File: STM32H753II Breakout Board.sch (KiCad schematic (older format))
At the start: 23 parts

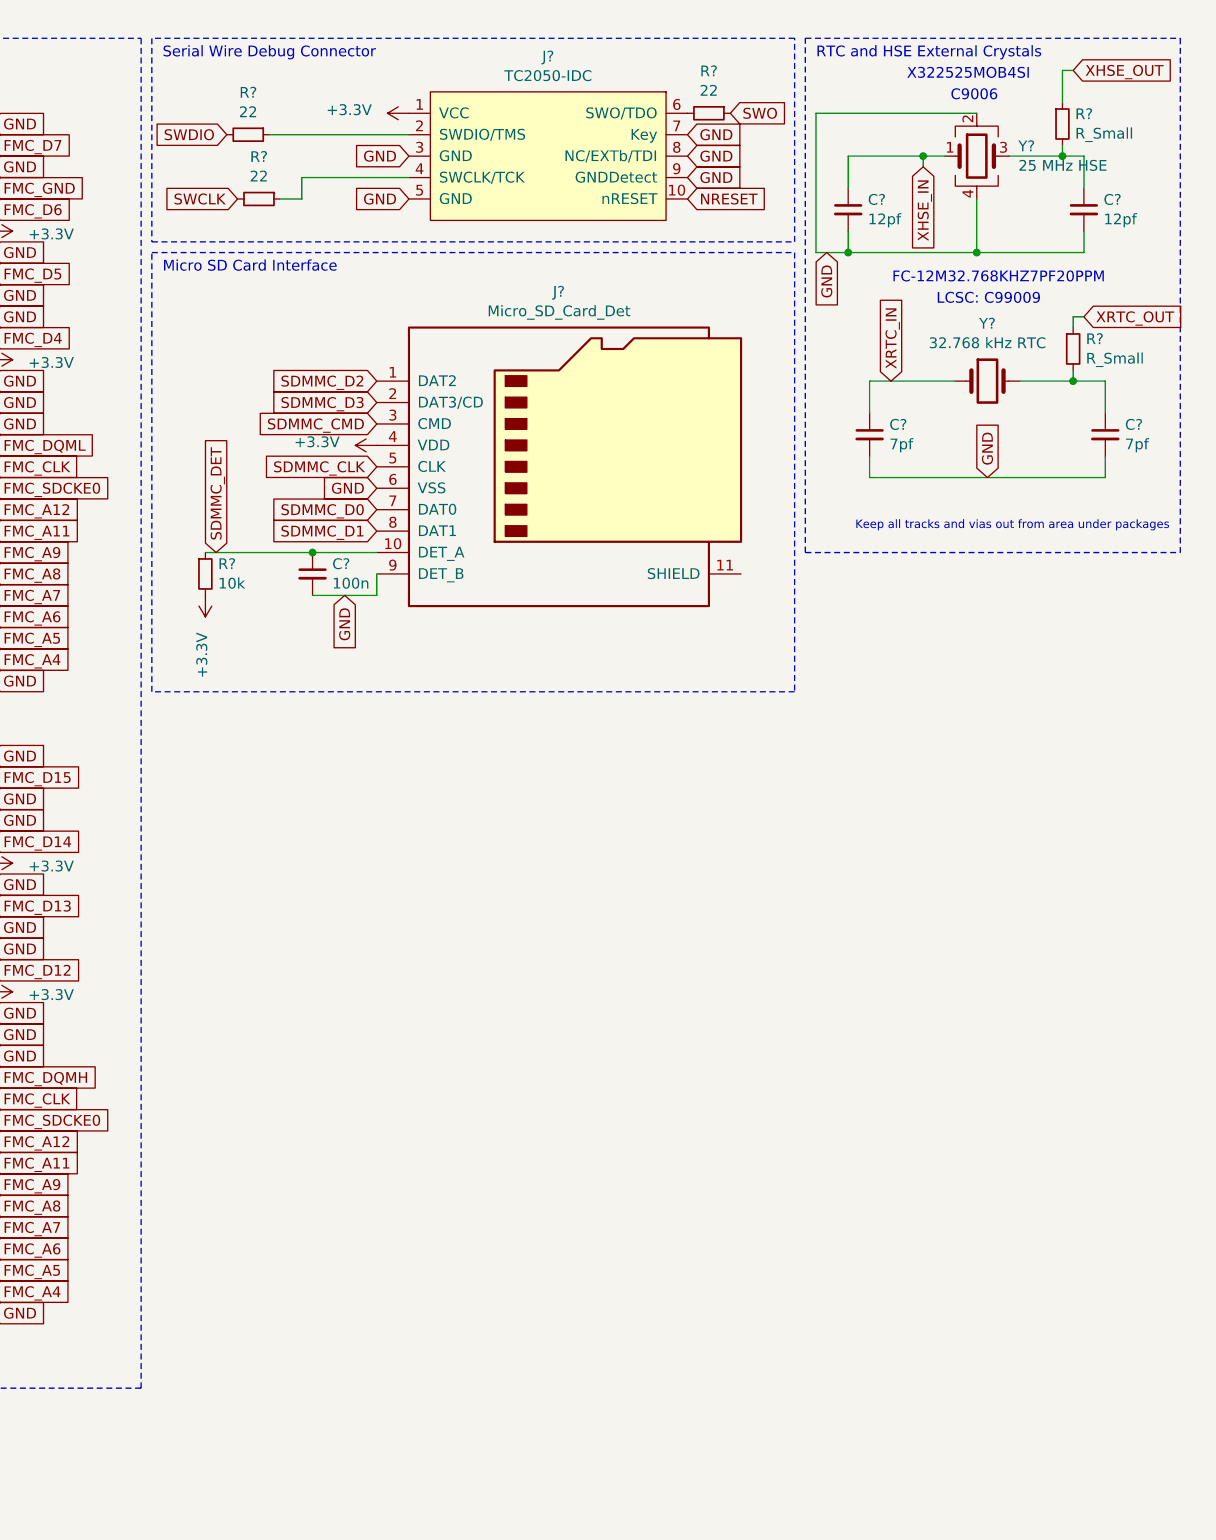
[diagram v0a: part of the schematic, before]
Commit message: added in switching regulator and drive fet symbols
Minor Update
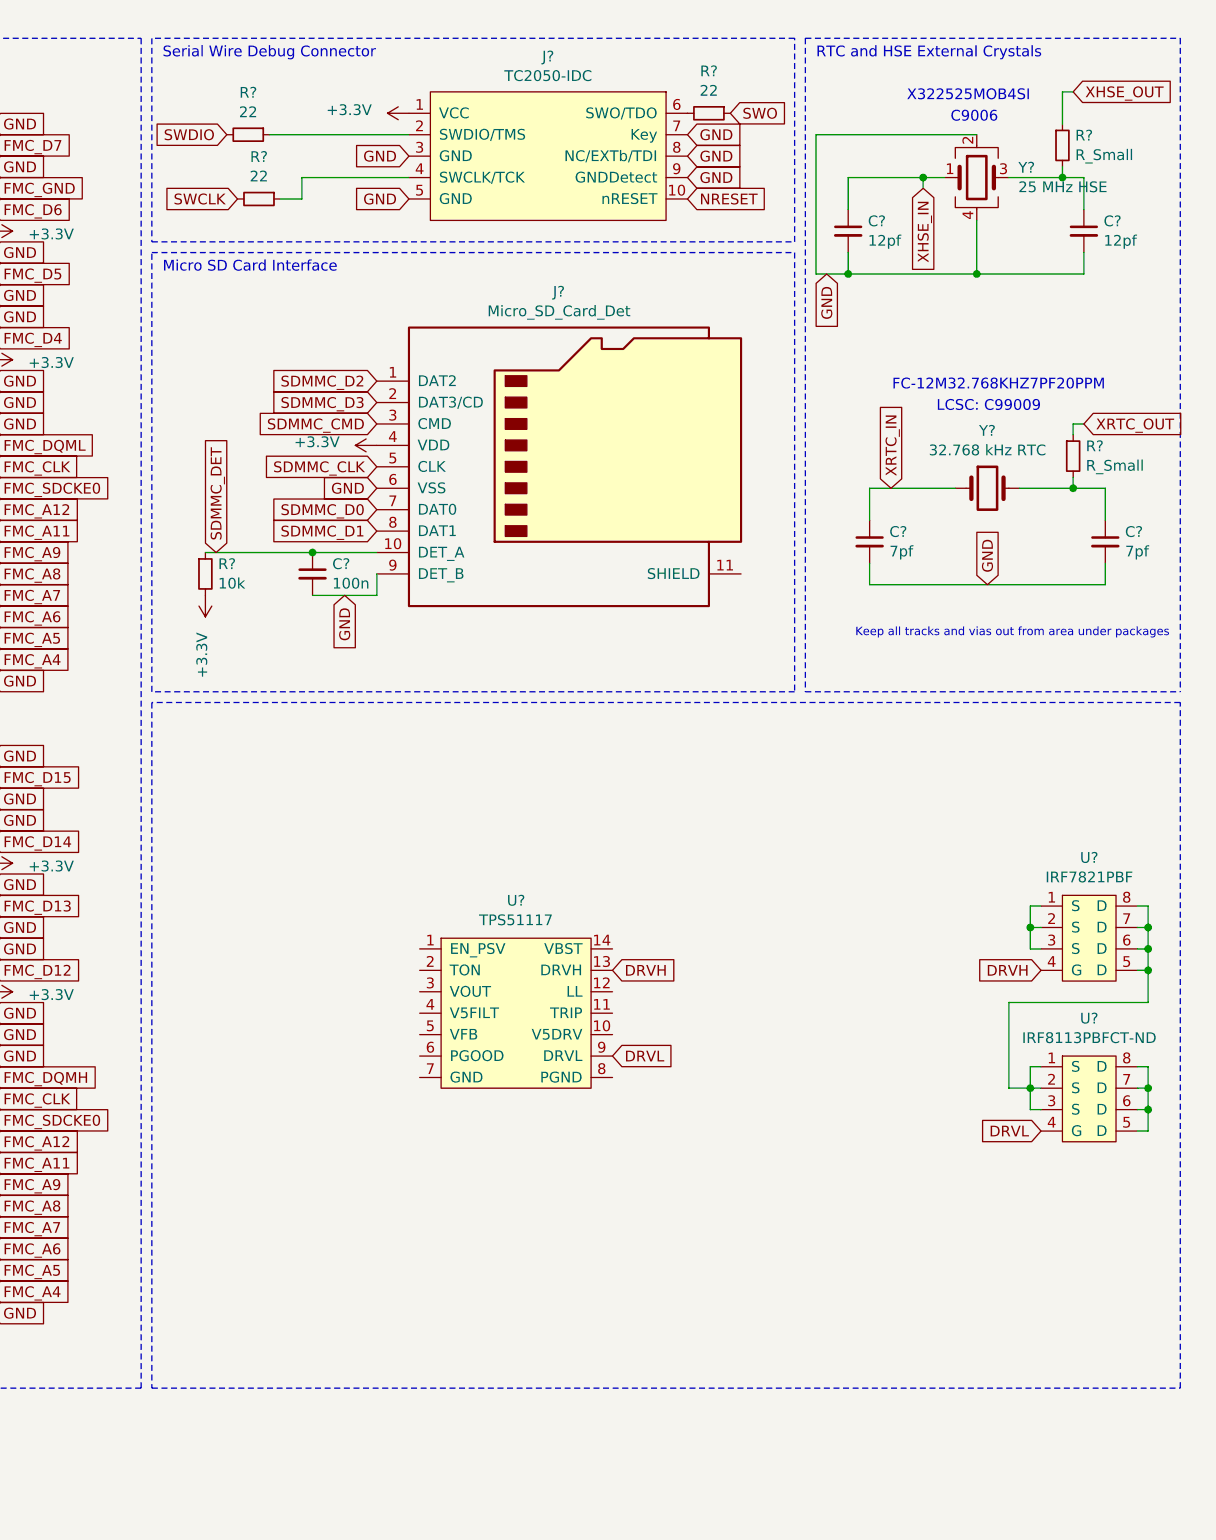
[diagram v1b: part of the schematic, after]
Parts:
- added U?: TPS51117, symbol SamacSys_Parts:TPS51117
- added U?: IRF7821PBF, symbol SamacSys_Parts:IRF7821PBF
- added U?: IRF8113PBFCT-ND, symbol SamacSys_Parts:IRF8113PBFCT-ND
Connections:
- new net: U?.1 (S), U?.2 (S), U?.3 (S)
- new net: U?.1 (S), U?.2 (S), U?.3 (S), U?.5 (D), U?.6 (D), U?.7 (D), U?.8 (D)
- new net: U?.5 (D), U?.6 (D), U?.7 (D), U?.8 (D)
- new net DRVH: U?.13 (DRVH), U?.4 (G)
- new net DRVL: U?.4 (G), U?.9 (DRVL)
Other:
- moved on the sheet: C?, R?, Y?

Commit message: Finished Laying out Components for Buck Converter
Component values are still needed.
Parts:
- added C1, C2, C3, C4: C_Small, symbol Device:C_Small
- added L1: L_Small, symbol Device:L_Small
- added R1, R2, R3, R4, R5, R6: R_Small, symbol Device:R_Small
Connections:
- net +3V3: now also U?.3 (VOUT), C1.2, L1.2, R1.1
- net +5V: now also U?.10 (V5DRV), U?.5 (D), U?.6 (D), U?.7 (D), U?.8 (D), C2.2, R5.1, R6.2
- net GND: now also R4.2
- net EN_PSV: now reaches U?.1 (EN_PSV)
- net at U?.11 (TRIP): now also R4.1
- net LL: now reaches U?.12 (LL)
- net LL: now also U?.1 (S), U?.2 (S), U?.3 (S), U?.5 (D), U?.6 (D), U?.7 (D), U?.8 (D), C4.1, L1.1, R3.1
- net at U?.14 (VBST): now also C4.2
- net at U?.2 (TON): now also R3.2
- net at U?.4 (V5FILT): now also C3.1, R5.2
- net VFB: now reaches U?.5 (VFB)
- net VFB: now also R1.2, R2.1
- net at U?.6 (PGOOD): now also R6.1
- net at U?.7 (GND): now also U?.1 (S), U?.2 (S), U?.3 (S), U?.8 (PGND), C1.1, C2.1, C3.2, R2.2
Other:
- note added: "DC-DC 3.3V Buck Converter"
- moved on the sheet: U?
